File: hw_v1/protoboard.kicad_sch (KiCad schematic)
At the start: 14 parts, among them J2 Conn_01x05, J3 Conn_01x05, J4 Conn_01x05, J5 Conn_01x03, J6 Conn_01x04

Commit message: wip sensors pcb layout
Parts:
- added TP17, TP18: TestPoint_Alt, TestPoint:TestPoint_THTPad_1.0x1.0mm_Drill0.5mm, symbol Connector:TestPoint_Alt
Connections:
- net ext_a0_in: now also TP17.1
- net ext_a1_in: now also TP18.1
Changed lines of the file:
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@@
+	)
+	(junction
+		(at 139.7 57.15)
+		(diameter 0)
+		(color 0 0 0 0)
 	)
 	(junction
@@
 	)
 	(junction
+		(at 143.51 59.69)
+		(diameter 0)
+		(color 0 0 0 0)
+	)
+	(junction
 		(at 63.5 119.38)
 		(diameter 0)
@@
 	(wire
 		(pts
+			(xy 139.7 57.15) (xy 148.59 57.15)
+		)
+		(stroke
+			(width 0)
+			(type default)
+		)
+	)
+	(wire
+		(pts
 			(xy 60.96 80.01) (xy 64.77 80.01)
 		)
@@
 	(wire
 		(pts
-			(xy 134.62 57.15) (xy 148.59 57.15)
+			(xy 134.62 57.15) (xy 139.7 57.15)
 		)
 		(stroke
@@
 	(wire
 		(pts
-			(xy 137.16 59.69) (xy 153.67 59.69)
+			(xy 137.16 59.69) (xy 143.51 59.69)
 		)
 		(stroke
@@
 		(pts
 			(xy 62.23 52.07) (xy 64.77 52.07)
+		)
+		(stroke
+			(width 0)
+			(type default)
+		)
+	)
+	(wire
+		(pts
+			(xy 143.51 59.69) (xy 153.67 59.69)
 		)
 		(stroke
@@
 	)
 	(symbol
+		(lib_id "Connector:TestPoint_Alt")
+		(at 143.51 59.69 0)
+		(unit 1)
+		(exclude_from_sim no)
+		(in_bom yes)
+		(on_board yes)
+		(dnp no)
+		(fields_autoplaced yes)
+		(property "Reference" "TP18"
+			(at 145.415 55.1179 0)
+			(effects
+				(font
+					(size 1.27 1.27)
+				)
+				(justify left)
+				(hide yes)
+			)
+		)
+		(property "Value" "TestPoint_Alt"
+			(at 145.415 57.6579 0)
+			(effects
+				(font
+					(size 1.27 1.27)
+				)
+				(justify left)
+				(hide yes)
+			)
+		)
+		(property "Footprint" "TestPoint:TestPoint_THTPad_1.0x1.0mm_Drill0.5mm"
+			(at 148.59 59.69 0)
+			(effects
+				(font
+					(size 1.27 1.27)
+				)
+				(hide yes)
+			)
+		)
+		(property "Datasheet" "~"
+			(at 148.59 59.69 0)
+			(effects
+				(font
+					(size 1.27 1.27)
+				)
+				(hide yes)
+			)
+		)
+		(property "Description" ""
+			(at 143.51 59.69 0)
+			(effects
+				(font
+					(size 1.27 1.27)
+				)
+				(hide yes)
+			)
+		)
+		(pin "1"
+		)
+		(instances
+			(project "hw_v1"
+				(path "/b3feb07e-be80-40e1-bd13-6cd54c2f8b0c/019e8a83-2b05-42df-8207-97dcaa5a8956"
+					(reference "TP18")
+					(unit 1)
+				)
+			)
+		)
+	)
+	(symbol
 		(lib_id "power:+5VA")
 		(at 137.16 43.18 0)
@@
 					(unit 1)
 				)
+			)
+		)
+	)
+	(symbol
+		(lib_id "Connector:TestPoint_Alt")
+		(at 139.7 57.15 0)
+		(unit 1)
+		(exclude_from_sim no)
+		(in_bom yes)
+		(on_board yes)
+		(dnp no)
+		(fields_autoplaced yes)
+		(property "Reference" "TP17"
+			(at 141.605 52.5779 0)
+			(effects
+				(font
+					(size 1.27 1.27)
+				)
+				(justify left)
+				(hide yes)
+			)
+		)
+		(property "Value" "TestPoint_Alt"
+			(at 141.605 55.1179 0)
+			(effects
+				(font
+					(size 1.27 1.27)
+				)
+				(justify left)
+				(hide yes)
+			)
+		)
+		(property "Footprint" "TestPoint:TestPoint_THTPad_1.0x1.0mm_Drill0.5mm"
+			(at 144.78 57.15 0)
+			(effects
+				(font
+					(size 1.27 1.27)
+				)
+				(hide yes)
+			)
+		)
+		(property "Datasheet" "~"
+			(at 144.78 57.15 0)
+			(effects
+				(font
+					(size 1.27 1.27)
+				)
+				(hide yes)
+			)
+		)
+		(property "Description" ""
+			(at 139.7 57.15 0)
+			(effects
+				(font
+					(size 1.27 1.27)
+				)
+				(hide yes)
+			)
+		)
+		(pin "1"
+		)
+		(instances
+			(project "hw_v1"
+				(path "/b3feb07e-be80-40e1-bd13-6cd54c2f8b0c/019e8a83-2b05-42df-8207-97dcaa5a8956"
+					(reference "TP17")
+					(unit 1)
+				)

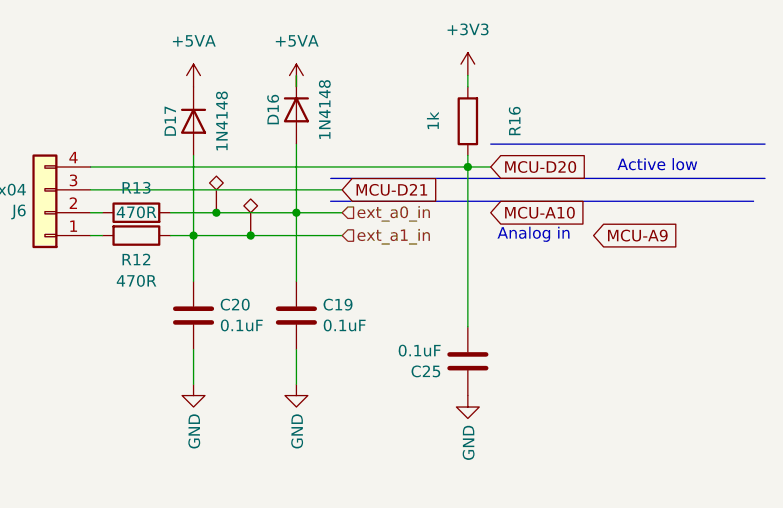
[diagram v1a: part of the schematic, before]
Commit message: wip sensors traces, added can
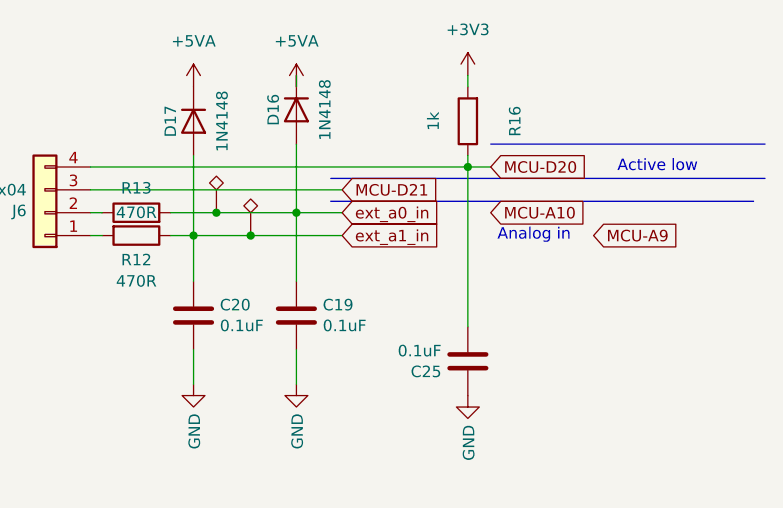
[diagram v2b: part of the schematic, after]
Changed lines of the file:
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@@
+		)
+	)
+	(global_label "ext_a1_in"
+		(shape input)
+		(at 153.67 59.69 0)
+		(fields_autoplaced yes)
+		(effects
+			(font
+				(size 1.27 1.27)
+			)
+			(justify left)
+		)
+		(property "Intersheetrefs" "${INTERSHEET_REFS}"
+			(at 165.5451 59.69 0)
+			(effects
+				(font
+					(size 1.27 1.27)
+				)
+				(justify left)
+				(hide yes)
+			)
 		)
 	)
@@
 					(size 1.27 1.27)
 				)
+				(hide yes)
+			)
+		)
+	)
+	(global_label "ext_a0_in"
+		(shape input)
+		(at 153.67 57.15 0)
+		(fields_autoplaced yes)
+		(effects
+			(font
+				(size 1.27 1.27)
+			)
+			(justify left)
+		)
+		(property "Intersheetrefs" "${INTERSHEET_REFS}"
+			(at 165.5451 57.15 0)
+			(effects
+				(font
+					(size 1.27 1.27)
+				)
+				(justify left)
 				(hide yes)
 			)
@@
 		)
 	)
-	(hierarchical_label "ext_a0_in"
-		(shape input)
-		(at 153.67 57.15 0)
-		(fields_autoplaced yes)
-		(effects
-			(font
-				(size 1.27 1.27)
-			)
-			(justify left)
-		)
-	)
-	(hierarchical_label "ext_a1_in"
-		(shape input)
-		(at 153.67 59.69 0)
-		(fields_autoplaced yes)
-		(effects
-			(font
-				(size 1.27 1.27)
-			)
-			(justify left)
-		)
-	)

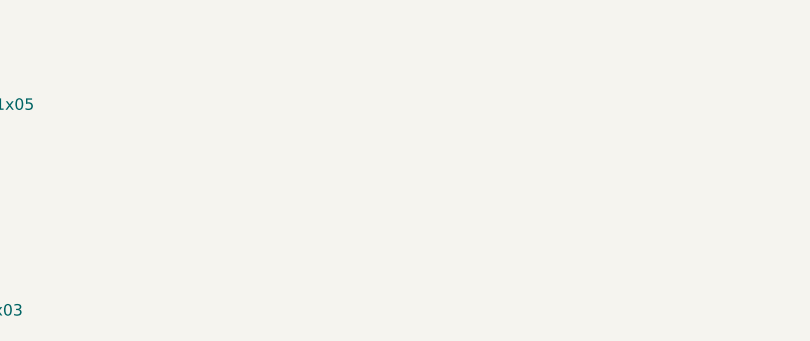
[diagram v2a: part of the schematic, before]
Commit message: placed al SMD, wip pmic traces
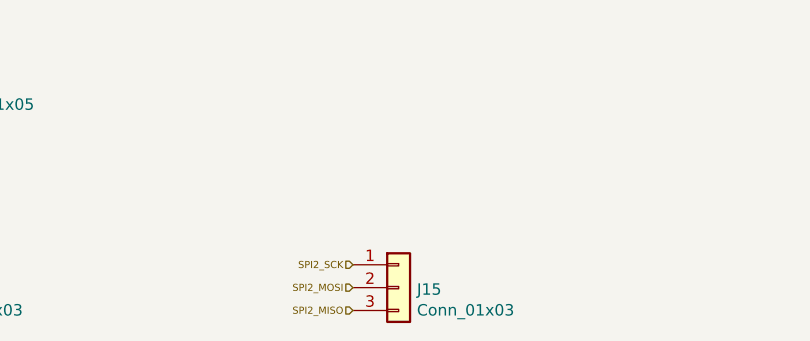
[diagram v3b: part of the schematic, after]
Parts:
- added J15: Conn_01x03, Connector_PinHeader_2.54mm:PinHeader_1x03_P2.54mm_Vertical, symbol Connector_Generic:Conn_01x03
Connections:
- new net SPI2_MISO: J15.3 (Pin_3)
- new net SPI2_MOSI: J15.2 (Pin_2)
- new net SPI2_SCK: J15.1 (Pin_1)
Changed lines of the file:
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@@
+		)
+	)
+	(hierarchical_label "SPI2_SCK"
+		(shape input)
+		(at 118.11 119.38 180)
+		(fields_autoplaced yes)
+		(effects
+			(font
+				(size 0.7874 0.7874)
+			)
+			(justify right)
+		)
+	)
+	(hierarchical_label "SPI2_MOSI"
+		(shape input)
+		(at 118.11 121.92 180)
+		(fields_autoplaced yes)
+		(effects
+			(font
+				(size 0.7874 0.7874)
+			)
+			(justify right)
+		)
+	)
+	(hierarchical_label "SPI2_MISO"
+		(shape input)
+		(at 118.11 124.46 180)
+		(fields_autoplaced yes)
+		(effects
+			(font
+				(size 0.7874 0.7874)
+			)
+			(justify right)
 		)
 	)
@@
 					(unit 1)
 				)
+			)
+		)
+	)
+	(symbol
+		(lib_id "Connector_Generic:Conn_01x03")
+		(at 123.19 121.92 0)
+		(unit 1)
+		(exclude_from_sim no)
+		(in_bom yes)
+		(on_board yes)
+		(dnp no)
+		(property "Reference" "J15"
+			(at 125.222 122.1232 0)
+			(effects
+				(font
+					(size 1.27 1.27)
+				)
+				(justify left)
+			)
+		)
+		(property "Value" "Conn_01x03"
+			(at 125.222 124.4346 0)
+			(effects
+				(font
+					(size 1.27 1.27)
+				)
+				(justify left)
+			)
+		)
+		(property "Footprint" "Connector_PinHeader_2.54mm:PinHeader_1x03_P2.54mm_Vertical"
+			(at 123.19 121.92 0)
+			(effects
+				(font
+					(size 1.27 1.27)
+				)
+				(hide yes)
+			)
+		)
+		(property "Datasheet" "~"
+			(at 123.19 121.92 0)
+			(effects
+				(font
+					(size 1.27 1.27)
+				)
+				(hide yes)
+			)
+		)
+		(property "Description" ""
+			(at 123.19 121.92 0)
+			(effects
+				(font
+					(size 1.27 1.27)
+				)
+				(hide yes)
+			)
+		)
+		(property "Sim.Device" "SPICE"
+			(at 123.19 121.92 0)
+			(effects
+				(font
+					(size 1.27 1.27)
+				)
+				(hide yes)
+			)
+		)
+		(property "Sim.Params" "type=\"J\" model=\"Conn_01x03\" lib=\"\""
+			(at -10.16 10.16 0)
+			(effects
+				(font
+					(size 1.27 1.27)
+				)
+				(hide yes)
+			)
+		)
+		(property "Sim.Pins" "1=1 2=2 3=3"
+			(at -10.16 10.16 0)
+			(effects
+				(font
+					(size 1.27 1.27)
+				)
+				(hide yes)
+			)
+		)
+		(pin "1"
+		)
+		(pin "2"
+		)
+		(pin "3"
+		)
+		(instances
+			(project "hw_v1"
+				(path "/b3feb07e-be80-40e1-bd13-6cd54c2f8b0c/019e8a83-2b05-42df-8207-97dcaa5a8956"
+					(reference "J15")
+					(unit 1)
+				)

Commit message: finish pcb layout
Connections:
- net +3V3: no longer F1.1
- net +5VA: now also F1.1
- net MCU-D20 renamed MCU-D0
- net MCU-D21 renamed MCU-D1
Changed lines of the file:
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@@
 		)
 	)
-	(global_label "MCU-D20"
+	(global_label "MCU-D0"
 		(shape input)
 		(at 170.18 52.07 0)
@@
 		)
 	)
-	(global_label "MCU-D21"
+	(global_label "MCU-D1"
 		(shape input)
 		(at 153.67 54.61 0)
@@
 	(symbol
 		(lib_id "power:+3V3")
-		(at 60.96 64.77 0)
-		(unit 1)
-		(exclude_from_sim no)
-		(in_bom yes)
-		(on_board yes)
-		(dnp no)
-		(fields_autoplaced yes)
-		(property "Reference" "#PWR045"
-			(at 60.96 68.58 0)
-			(effects
-				(font
-					(size 1.27 1.27)
-				)
-				(hide yes)
-			)
-		)
-		(property "Value" "+3V3"
-			(at 60.96 59.69 0)
-			(effects
-				(font
-					(size 1.27 1.27)
-				)
-			)
-		)
-		(property "Footprint" ""
-			(at 60.96 64.77 0)
-			(effects
-				(font
-					(size 1.27 1.27)
-				)
-				(hide yes)
-			)
-		)
-		(property "Datasheet" ""
-			(at 60.96 64.77 0)
-			(effects
-				(font
-					(size 1.27 1.27)
-				)
-				(hide yes)
-			)
-		)
-		(property "Description" "Power symbol creates a global label with name \"+3V3\""
-			(at 60.96 64.77 0)
-			(effects
-				(font
-					(size 1.27 1.27)
-				)
-				(hide yes)
-			)
-		)
-		(pin "1"
-		)
-		(instances
-			(project "hw_v1"
-				(path "/b3feb07e-be80-40e1-bd13-6cd54c2f8b0c/019e8a83-2b05-42df-8207-97dcaa5a8956"
-					(reference "#PWR045")
-					(unit 1)
-				)
-			)
-		)
-	)
-	(symbol
-		(lib_id "power:+3V3")
 		(at 167.64 41.91 0)
 		(unit 1)
@@
 					(unit 1)
 				)
+			)
+		)
+	)
+	(symbol
+		(lib_id "power:+5VA")
+		(at 60.96 64.77 0)
+		(unit 1)
+		(exclude_from_sim no)
+		(in_bom yes)
+		(on_board yes)
+		(dnp no)
+		(fields_autoplaced yes)
+		(property "Reference" "#PWR0153"
+			(at 60.96 68.58 0)
+			(effects
+				(font
+					(size 1.27 1.27)
+				)
+				(hide yes)
+			)
+		)
+		(property "Value" "+5VA"
+			(at 60.96 59.69 0)
+			(effects
+				(font
+					(size 1.27 1.27)
+				)
+			)
+		)
+		(property "Footprint" ""
+			(at 60.96 64.77 0)
+			(effects
+				(font
+					(size 1.27 1.27)
+				)
+				(hide yes)
+			)
+		)
+		(property "Datasheet" ""
+			(at 60.96 64.77 0)
+			(effects
+				(font
+					(size 1.27 1.27)
+				)
+				(hide yes)
+			)
+		)
+		(property "Description" "Power symbol creates a global label with name \"+5VA\""
+			(at 60.96 64.77 0)
+			(effects
+				(font
+					(size 1.27 1.27)
+				)
+				(hide yes)
+			)
+		)
+		(pin "1"
+		)
+		(instances
+			(project "hw_v1"
+				(path "/b3feb07e-be80-40e1-bd13-6cd54c2f8b0c/019e8a83-2b05-42df-8207-97dcaa5a8956"
+					(reference "#PWR0153")
+					(unit 1)
+				)

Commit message: update SD card holder to Molex 47352
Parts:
- J15, J2, J3, J4, J5, J6, TP17, TP18: now left out of the parts list
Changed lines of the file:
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@@
 	(version 20231120)
 	(generator "eeschema")
-	(generator_version "7.99")
+	(generator_version "8.0")
 	(paper "A4")
 	(title_block
 		(title "μEFI (Speeduino FW compatible)")
 		(date "2023-12-25")
-		(rev "v6")
+		(rev "v6.1")
 		(company "Churrosoft ®")
-		(comment 1 "CERN-OHL-S-2.0 license\n")
+		(comment 1 "CERN-OHL-S-2.0 license")
 	)
 	(junction
@@
 		(unit 1)
 		(exclude_from_sim no)
-		(in_bom yes)
+		(in_bom no)
 		(on_board yes)
 		(dnp no)
@@
 		(unit 1)
 		(exclude_from_sim no)
-		(in_bom yes)
+		(in_bom no)
 		(on_board yes)
 		(dnp no)
@@
 		(unit 1)
 		(exclude_from_sim no)
-		(in_bom yes)
+		(in_bom no)
 		(on_board yes)
 		(dnp no)
@@
 		(unit 1)
 		(exclude_from_sim no)
-		(in_bom yes)
+		(in_bom no)
 		(on_board yes)
 		(dnp no)
@@
 		(unit 1)
 		(exclude_from_sim no)
-		(in_bom yes)
+		(in_bom no)
 		(on_board yes)
 		(dnp no)
@@
 		(unit 1)
 		(exclude_from_sim no)
-		(in_bom yes)
+		(in_bom no)
 		(on_board yes)
 		(dnp no)
@@
 		(unit 1)
 		(exclude_from_sim no)
-		(in_bom yes)
+		(in_bom no)
 		(on_board yes)
 		(dnp no)
@@
 		(unit 1)
 		(exclude_from_sim no)
-		(in_bom yes)
+		(in_bom no)
 		(on_board yes)
 		(dnp no)

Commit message: update vr inputs
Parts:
- R16: footprint Resistor_SMD:R_0805_2012Metric -> Resistor_SMD:R_0603_1608Metric; LCSC (none) -> C21190
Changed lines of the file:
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@@
 			)
 		)
-		(property "Footprint" "Resistor_SMD:R_0805_2012Metric"
+		(property "Footprint" "Resistor_SMD:R_0603_1608Metric"
 			(at 169.418 46.99 90)
 			(effects
@@
 			(effects
 				(font
+					(size 1.27 1.27)
+				)
+				(hide yes)
+			)
+		)
+		(property "LCSC" "C21190"
+			(at 167.64 46.99 90)
+			(effects
+				(font

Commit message: update footprints
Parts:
- D16, D17: LCSC C511874 -> C5277952
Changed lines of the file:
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@@
 			)
 		)
-		(property "LCSC" "C511874"
+		(property "LCSC" "C5277952"
 			(at 137.16 46.99 0)
 			(effects
@@
 			)
 		)
-		(property "LCSC" "C511874"
+		(property "LCSC" "C5277952"
 			(at 148.59 45.72 0)
 			(effects

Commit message: update from inventree
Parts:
- C19, C20, C25: LCSC (none) -> C49678; STOCK (none) -> CAP-000175-00
- D16, D17: value 1N4148 -> 1N5819WS; footprint Diode_SMD:D_SOD-523 -> Diode_SMD:D_SOD-323_HandSoldering; LCSC C5277952 -> C191023; STOCK (none) -> DIO-000272-00
- F1: LCSC (none) -> -; STOCK (none) -> -
- J15, J2, J3, J4, J5, J6, TP17, TP18: now not fitted
- R12, R13: LCSC (none) -> C114564; STOCK (none) -> RES-000077-00
- R16: STOCK (none) -> RES-000107-00
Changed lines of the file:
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@@
 		(in_bom no)
 		(on_board yes)
-		(dnp no)
+		(dnp yes)
 		(property "Reference" "J6"
 			(at 118.618 56.9468 0)
@@
 		(in_bom no)
 		(on_board yes)
-		(dnp no)
+		(dnp yes)
 		(fields_autoplaced yes)
 		(property "Reference" "TP18"
@@
 		(in_bom no)
 		(on_board yes)
-		(dnp no)
+		(dnp yes)
 		(property "Reference" "J2"
 			(at 71.882 80.2132 0)
@@
 		(in_bom no)
 		(on_board yes)
-		(dnp no)
+		(dnp yes)
 		(property "Reference" "J15"
 			(at 125.222 122.1232 0)
@@
 		(in_bom no)
 		(on_board yes)
-		(dnp no)
+		(dnp yes)
 		(fields_autoplaced yes)
 		(property "Reference" "TP17"
@@
 		(in_bom no)
 		(on_board yes)
-		(dnp no)
+		(dnp yes)
 		(property "Reference" "J4"
 			(at 71.882 99.2632 0)
@@
 		(property "URL" "https://www.digikey.com.au/product-detail/en/yageo/CC0805KRX7R9BB104/311-1140-1-ND/303050"
 			(at 1.27 134.62 0)
+			(effects
+				(font
+					(size 1.27 1.27)
+				)
+				(hide yes)
+			)
+		)
+		(property "LCSC" "C49678"
+			(at 148.59 68.58 0)
+			(effects
+				(font
+					(size 1.27 1.27)
+				)
+				(hide yes)
+			)
+		)
+		(property "STOCK" "CAP-000175-00"
+			(at 148.59 68.58 0)
 			(effects
 				(font
@@
 		(in_bom no)
 		(on_board yes)
-		(dnp no)
+		(dnp yes)
 		(property "Reference" "J3"
 			(at 71.882 47.1932 0)
@@
 		(in_bom no)
 		(on_board yes)
-		(dnp no)
+		(dnp yes)
 		(property "Reference" "J5"
 			(at 70.612 122.1232 0)
@@
 			)
 		)
-		(property "Value" "1N4148"
+		(property "Value" "1N5819WS"
 			(at 140.3604 46.99 0)
 			(effects
@@
 			)
 		)
-		(property "Footprint" "Diode_SMD:D_SOD-523"
+		(property "Footprint" "Diode_SMD:D_SOD-323_HandSoldering"
 			(at 132.715 46.99 0)
 			(effects
@@
 			)
 		)
-		(property "LCSC" "C5277952"
+		(property "LCSC" "C191023"
 			(at 137.16 46.99 0)
 			(effects
 				(font
 					(size 0.889 0.889)
+				)
+				(hide yes)
+			)
+		)
+		(property "STOCK" "DIO-000272-00"
+			(at 137.16 46.99 0)
+			(effects
+				(font
+					(size 1.27 1.27)
 				)
 				(hide yes)
@@
 		(property "URL" "https://www.digikey.com.au/product-detail/en/yageo/CC0805KRX7R9BB104/311-1140-1-ND/303050"
 			(at -30.48 134.62 0)
+			(effects
+				(font
+					(size 1.27 1.27)
+				)
+				(hide yes)
+			)
+		)
+		(property "LCSC" "C49678"
+			(at 137.16 68.58 0)
+			(effects
+				(font
+					(size 1.27 1.27)
+				)
+				(hide yes)
+			)
+		)
+		(property "STOCK" "CAP-000175-00"
+			(at 137.16 68.58 0)
 			(effects
 				(font
@@
 			)
 		)
+		(property "STOCK" "RES-000107-00"
+			(at 167.64 46.99 0)
+			(effects
+				(font
+					(size 1.27 1.27)
+				)
+				(hide yes)
+			)
+		)
 		(pin "1"
 		)
@@
 			)
 		)
+		(property "LCSC" "-"
+			(at 60.96 68.58 0)
+			(effects
+				(font
+					(size 1.27 1.27)
+				)
+				(hide yes)
+			)
+		)
+		(property "STOCK" "-"
+			(at 60.96 68.58 0)
+			(effects
+				(font
+					(size 1.27 1.27)
+				)
+				(hide yes)
+			)
+		)
 		(pin "1"
 		)
@@
 			)
 		)
+		(property "LCSC" "C114564"
+			(at 130.81 59.69 0)
+			(effects
+				(font
+					(size 1.27 1.27)
+				)
+				(hide yes)
+			)
+		)
+		(property "STOCK" "RES-000077-00"
+			(at 130.81 59.69 0)
+			(effects
+				(font
+					(size 1.27 1.27)
+				)
+				(hide yes)
+			)
+		)
 		(pin "2"
 		)
@@
 			)
 		)
+		(property "LCSC" "C49678"
+			(at 167.64 73.66 0)
+			(effects
+				(font
+					(size 1.27 1.27)
+				)
+				(hide yes)
+			)
+		)
+		(property "STOCK" "CAP-000175-00"
+			(at 167.64 73.66 0)
+			(effects
+				(font
+					(size 1.27 1.27)
+				)
+				(hide yes)
+			)
+		)
 		(pin "1"
 		)
@@
 			)
 		)
+		(property "LCSC" "C114564"
+			(at 130.81 57.15 0)
+			(effects
+				(font
+					(size 1.27 1.27)
+				)
+				(hide yes)
+			)
+		)
+		(property "STOCK" "RES-000077-00"
+			(at 130.81 57.15 0)
+			(effects
+				(font
+					(size 1.27 1.27)
+				)
+				(hide yes)
+			)
+		)
 		(pin "1"
 		)
@@
 			)
 		)
-		(property "Value" "1N4148"
+		(property "Value" "1N5819WS"
 			(at 151.7904 45.72 0)
 			(effects
@@
 			)
 		)
-		(property "Footprint" "Diode_SMD:D_SOD-523"
+		(property "Footprint" "Diode_SMD:D_SOD-323_HandSoldering"
 			(at 144.145 45.72 0)
 			(effects
@@
 			)
 		)
-		(property "LCSC" "C5277952"
+		(property "LCSC" "C191023"
 			(at 148.59 45.72 0)
 			(effects
@@
 				)
 				(hide yes)
+			)
+		)
+		(property "STOCK" "DIO-000272-00"
+			(at 148.59 45.72 0)
+			(effects
+				(font
+					(size 1.27 1.27)
+				)
+				(hide yes)
